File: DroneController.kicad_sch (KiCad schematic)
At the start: 68 parts, among them P1 USB_C_Plug, Q2 AO3400A, Q3 AO3400A, SW2 SW_SPDT, U1 ICM-42605, U2 W25Q16JVSS, U3 BMP280, U5 STM32F411, U6 L86-M33, U7 915MHz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

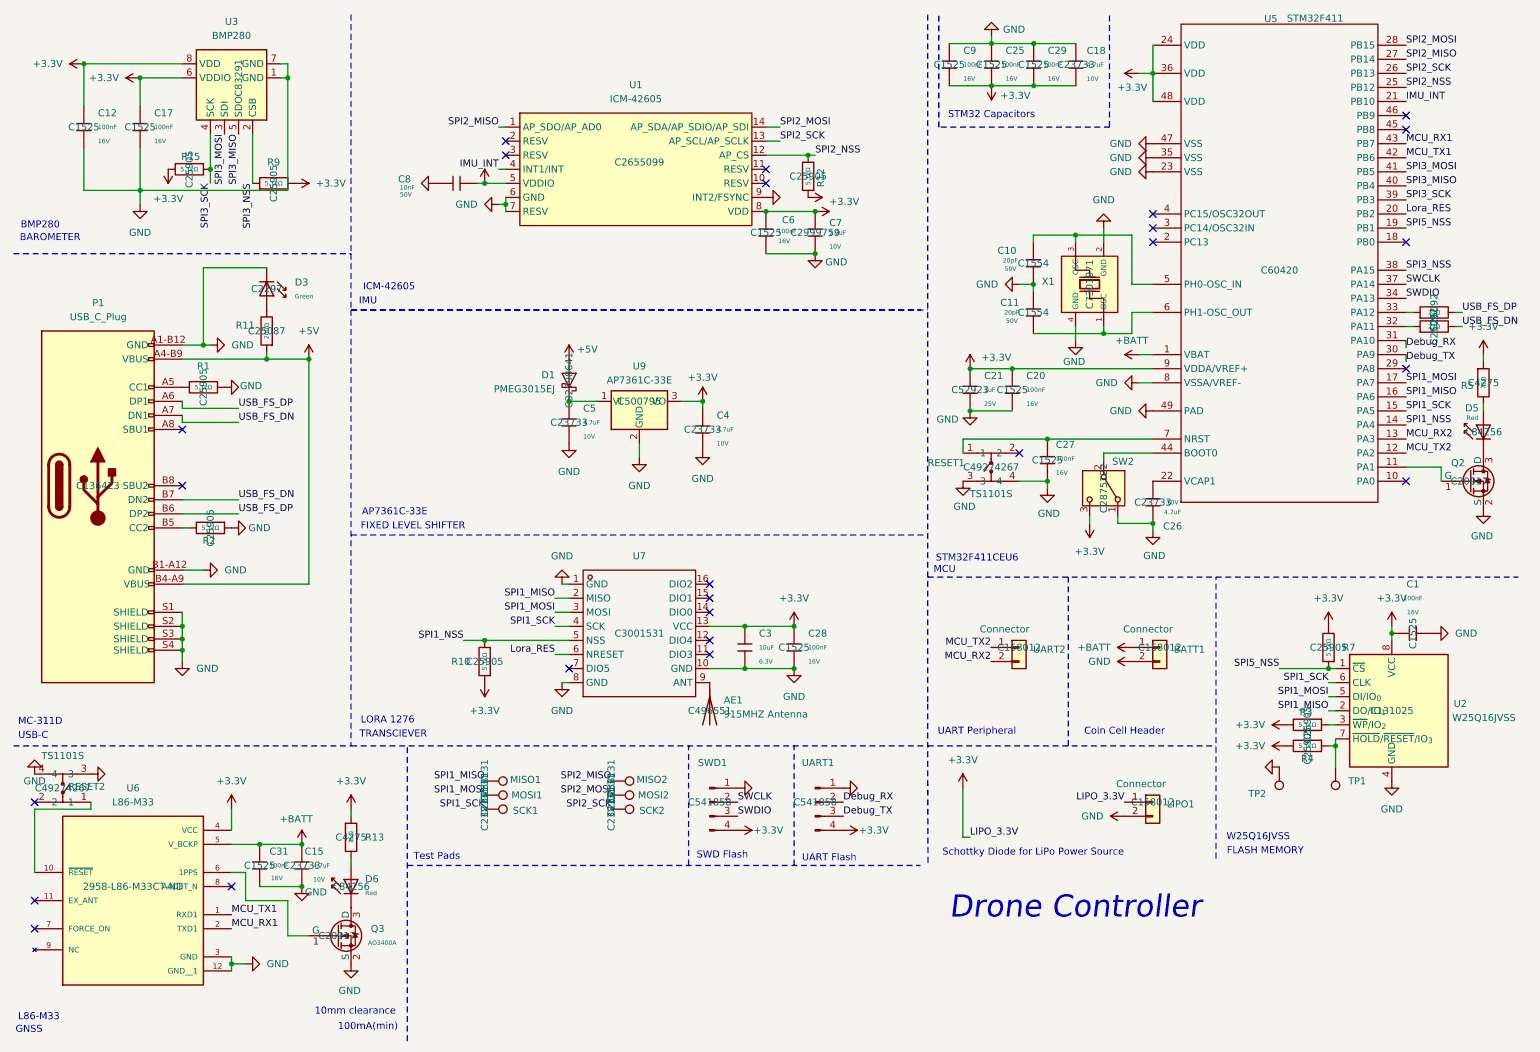
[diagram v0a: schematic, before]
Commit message: Modified BMP280 wiring, cleaned up schematic
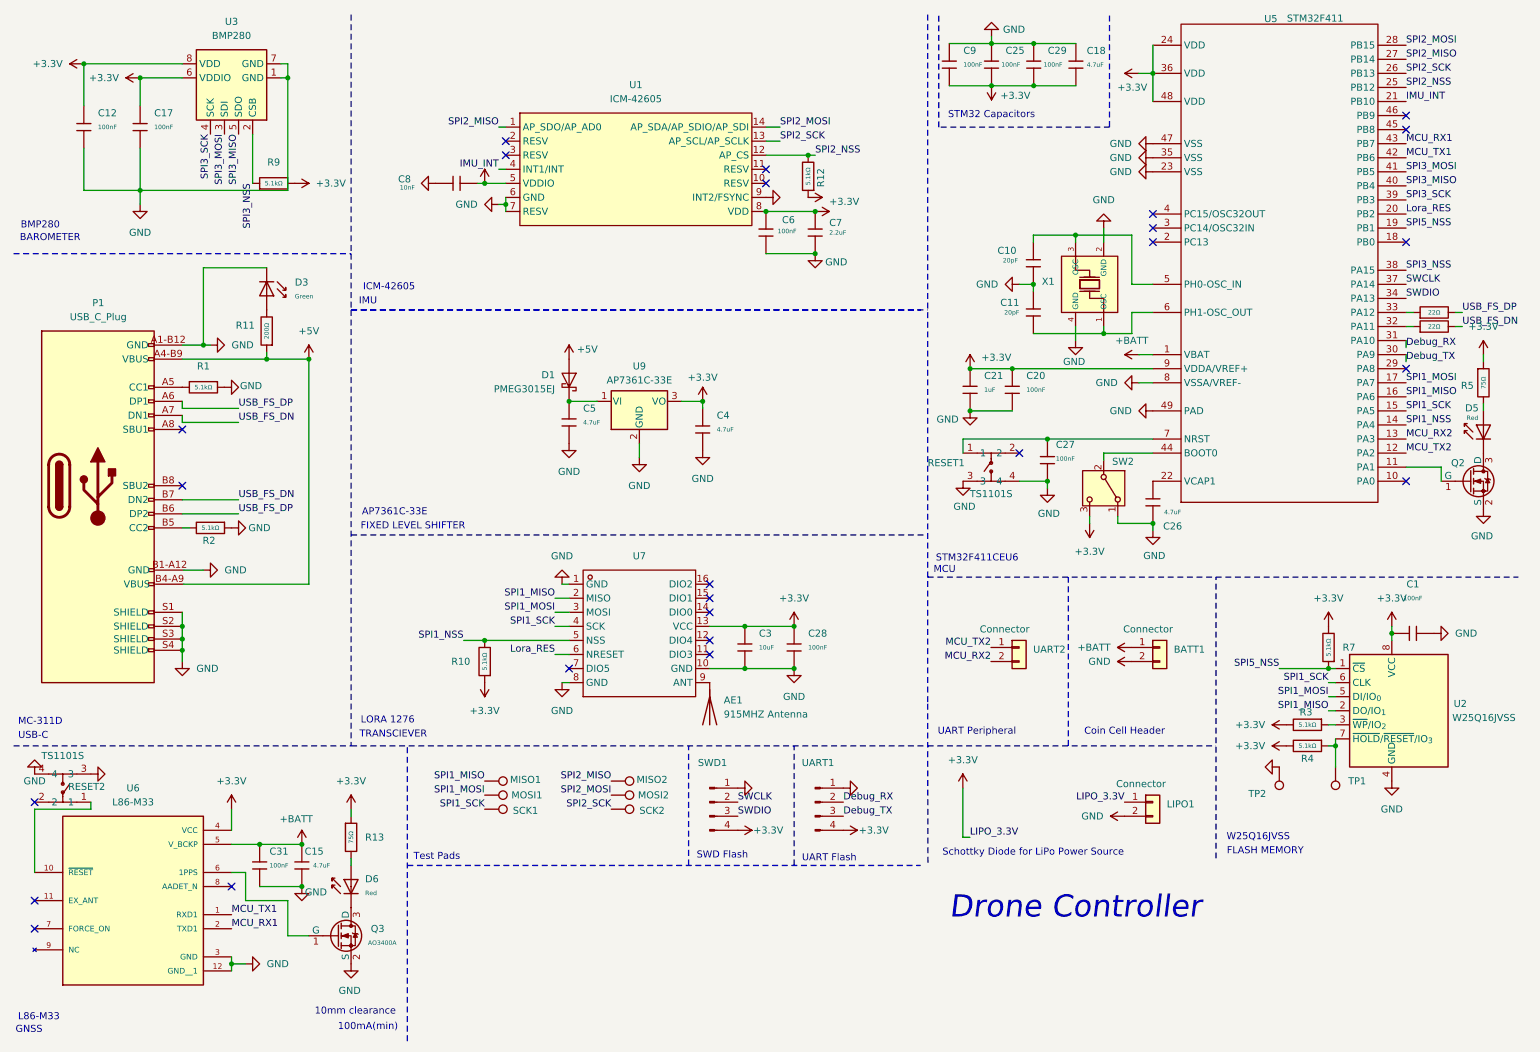
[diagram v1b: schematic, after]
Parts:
- removed R15: 5.1kΩ, PCM_JLCPCB:R_0402, symbol PCM_JLCPCB-Resistors:0402,5.1kΩ
